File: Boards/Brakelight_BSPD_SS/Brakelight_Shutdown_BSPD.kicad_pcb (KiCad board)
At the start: 2 copper layers, 59.2 x 76.3 mm, 84 parts, among them IC1 ATMEGA16M1, J2 MM_F_RA_20, J3 CONN_02X03, Q1 SSM3K333R, Q2 SSM3K333R, Q3 SSM3K333R, Q6 SSM3K333R, U1 SN74LVC1G08, U101 TPS560430YF, U2 MCP6001, U3 CAN_Transceiver, U4 MCP6001, U5 SN74LVC1G02, U6 SN74LVC1G02, U7 MCP6001, U8 SN74LVC1G32, Y1 Crystal_SMD

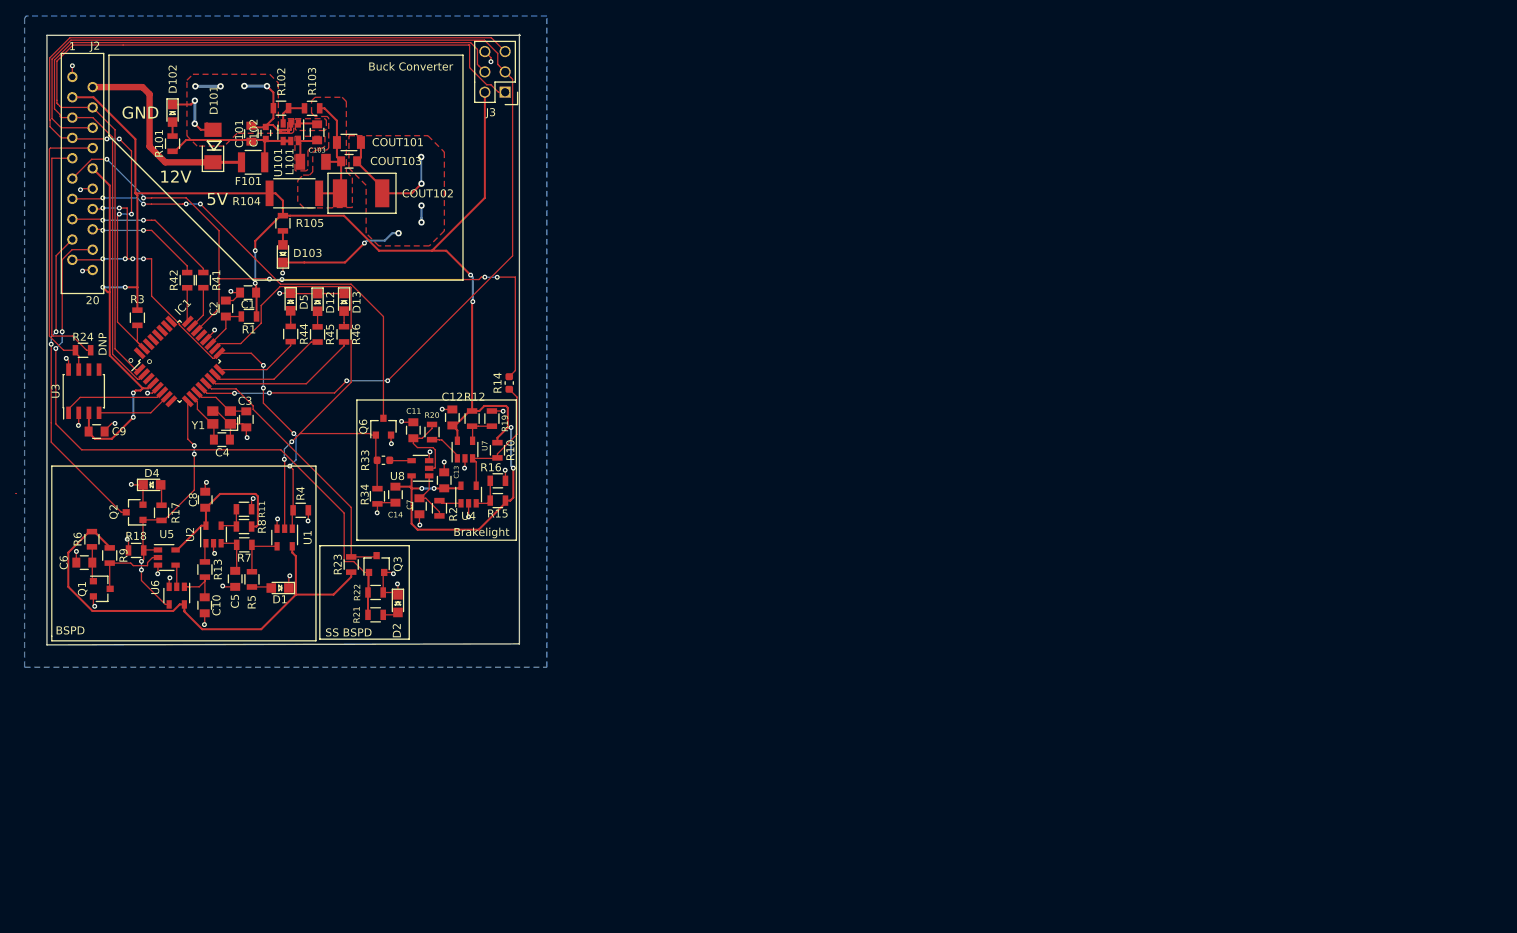
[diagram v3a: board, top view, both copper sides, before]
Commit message: Update BSPD layout with new PCB shape
There is now a large empty space on the board for
text and/or pictures.
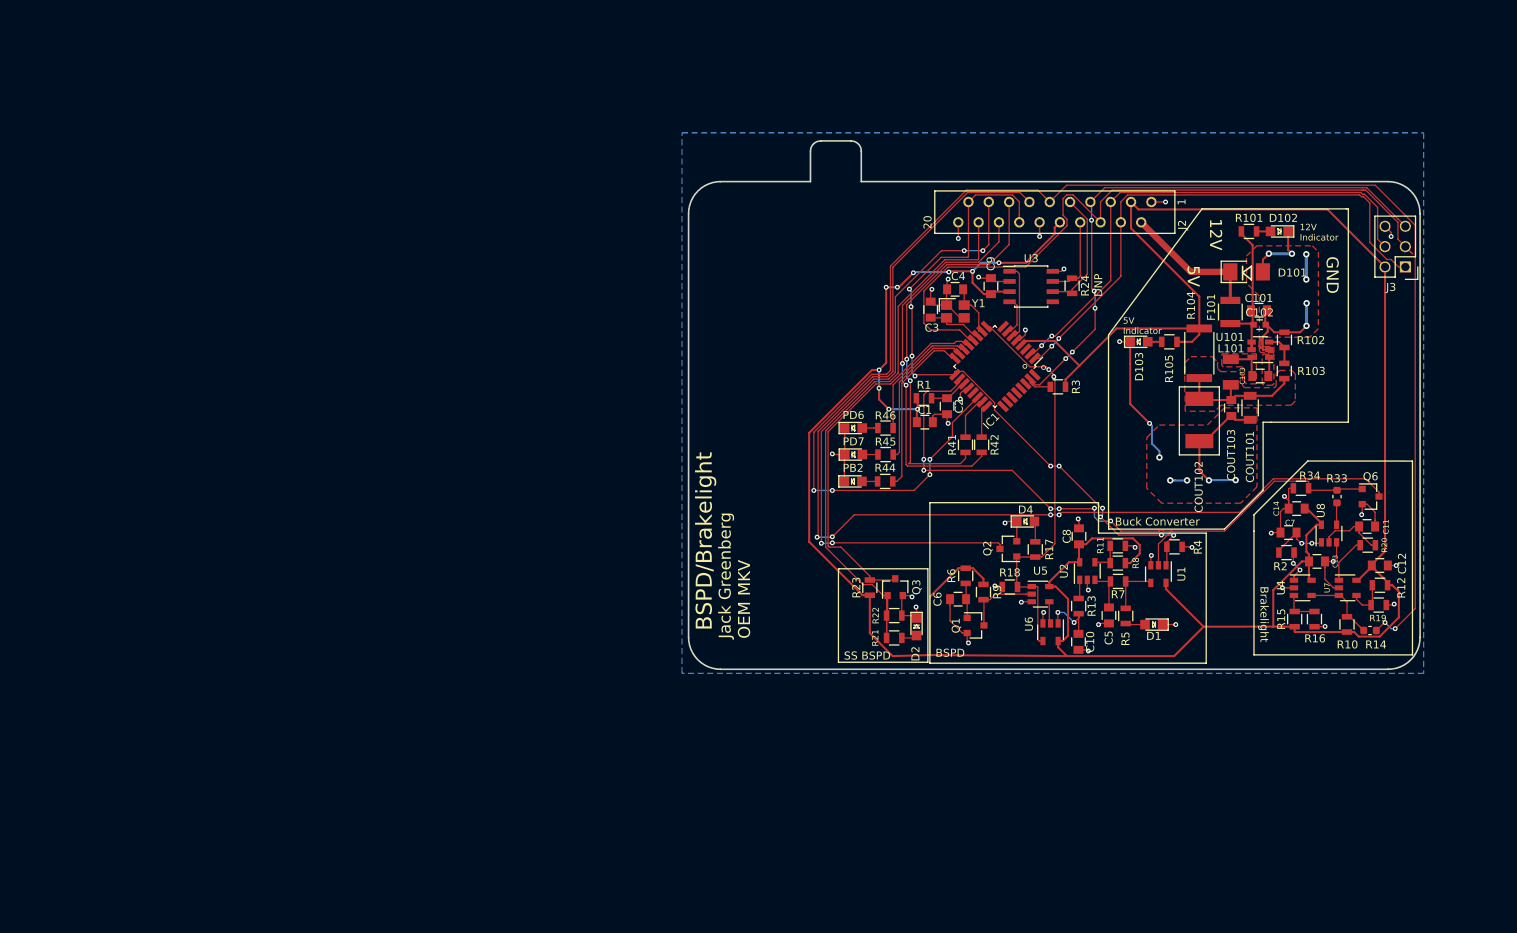
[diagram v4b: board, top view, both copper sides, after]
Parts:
- removed D12, D13, D5: LED_0805, footprints:LED_0805_OEM
- added G***: LOGO, footprints:Logo_Large, B.Cu at (110.7, 69.6)
- added PB2: LED_0805, footprints:LED_0805_OEM, F.Cu at (123.0, 77.9)
- added PD6: LED_0805, footprints:LED_0805_OEM, F.Cu at (123.0, 71.2)
- added PD7: LED_0805, footprints:LED_0805_OEM, F.Cu at (123.1, 74.5)
- moved D102 139.1 mm to (176.3, 46.6), turned to 180 degrees
- moved R101 135.0 mm to (172.5, 46.6), turned to 0 degrees
- moved J2 130.2 mm to (155.2, 42.9), turned to 270 degrees
- moved D101 130.2 mm to (172.2, 51.7), turned to 0 degrees
- moved R102 128.7 mm to (176.9, 60.2), turned to 90 degrees
- moved C101 127.9 mm to (173.7, 56.5), turned to 0 degrees
- moved C102 126.5 mm to (173.8, 58.3), turned to 0 degrees
- moved R103 125.9 mm to (176.9, 64.1), turned to 90 degrees
- moved U101 124.2 mm to (173.9, 61.4), turned to 180 degrees
- moved R24 123.9 mm to (150.4, 53.4), turned to 270 degrees
- moved Q6 123.7 mm to (187.7, 79.8), turned to 0 degrees
- moved F101 123.6 mm to (170.1, 56.7), turned to 90 degrees
- moved C103 121.8 mm to (173.9, 64.7), turned to 0 degrees
- moved C11 119.8 mm to (187.2, 83.5), turned to 0 degrees
- moved R33 119.3 mm to (183.5, 79.8), turned to 270 degrees
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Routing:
- net /BRAKE_PRESSURE_SENSE: track 86.8 -> 188.2 mm
- net /BRAKELIGHT_LSD: track 57.8 -> 134.7 mm
- net VCC: track 316.5 -> 380.1 mm, vias 12 -> 10
- net /SCK: track 142.8 -> 88.9 mm, vias 4 -> 0
- net /MOSI: track 104.9 -> 63.6 mm, vias 0 -> 2
- net /MISO: track 106.5 -> 67.3 mm, vias 0 -> 2
- net /BSPD_RELAY_LSD: track 39.4 -> 78.4 mm, vias 2 -> 4
- net /RESET: track 109.7 -> 72.5 mm, vias 4 -> 5
- net /RJ45_LED_O: track 14.5 -> 48.4 mm
- net /RJ45_LED_G: track 19.4 -> 49.5 mm
- net /CAN_HIGH: track 35.4 -> 10.5 mm
- net GND: track 143.3 -> 162.6 mm, vias 52 -> 48
- net /BSPD_RELAY_INTENTION: track 33.7 -> 51.3 mm, vias 4 -> 2
- net /BSPD_CURRENT_SENSE: track 66.1 -> 83.7 mm
- net /CAN_LOW: track 30.3 -> 15.6 mm
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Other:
- board size 59.2 x 76.3 mm -> 91.4 x 66 mm
- board text added: "12V Indicator"
- board text added: "5V Indicator"
- board text added: "BSPD/Brakelight"
- board text added: "Jack Greenberg OEM MKV"

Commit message: Schematics Edits
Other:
- board text added: "Rev 1"
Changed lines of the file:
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@@
   (general
     (thickness 1.6)
-    (drawings 57)
+    (drawings 58)
     (tracks 893)
     (zones 0)
@@
     )
   )
+  (gr_text "Rev 1" (at 111.76 94.234 90) (layer F.SilkS)
+    (effects (font (size 1.5 1.5) (thickness 0.2)))
+  )
   (gr_text "5V\nIndicator" (at 156.718 58.42) (layer F.SilkS)

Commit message: BSPD Rev 1 finished
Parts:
- moved J3 48.8 mm to (183.1, 99.1), turned to 90 degrees
- moved C13 5.06 mm to (179.5, 83.0)
- moved C14 5.06 mm to (176.9, 76.4)
- moved R12 5.06 mm to (187.3, 86.0)
- moved R19 5.06 mm to (187.2, 88.5)
- moved C11 5.06 mm to (185.7, 78.7)
- moved C12 5.06 mm to (187.3, 83.5)
- moved C7 5.06 mm to (175.9, 79.4)
- moved Q6 5.06 mm to (186.2, 74.9)
- moved R10 5.06 mm to (183.2, 90.9)
- moved R14 5.06 mm to (186.1, 91.7)
- moved R15 5.06 mm to (176.7, 90.2)
- moved R16 5.06 mm to (179.1, 90.3)
- moved R2 5.06 mm to (175.6, 81.9)
- moved R20 5.06 mm to (185.8, 81.0)
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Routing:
- net /SCK: track 88.9 -> 146.9 mm
- net /RESET: track 72.5 -> 130.3 mm
- net /MOSI: track 63.6 -> 120.0 mm
- net /MISO: track 67.3 -> 123.6 mm
- net VCC: track 380.1 -> 398.0 mm
- net /BRAKELIGHT_LSD: track 134.7 -> 138.5 mm
- net /BRAKELIGHT_GATE: track 82.3 -> 85.1 mm
- net /BRAKE_PRESSURE_SENSE: track 188.2 -> 186.2 mm, vias 6 -> 10
- net +12V: track 17.6 -> 16.1 mm
- net GND: track 162.6 -> 161.5 mm, vias 48 -> 49
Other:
- board text added: "Debug LEDs"
- board text added: "Jack Greenberg BSPD/Brakelight Rev 1 | 12/02/19 OEM - MKV"
- board text removed: "BSPD/Brakelight"
- board text removed: "Jack Greenberg OEM MKV"
- board text removed: "Rev 1"
